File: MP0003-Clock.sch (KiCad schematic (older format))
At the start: 43 parts, among them J1 Conn_01x02, J2 Conn_01x06, J3 Conn_01x06, SW1 HOLD, SW2 SW_Push_DPDT_8x8, SW3 RESET, U1 NE555P, U2 74HC00, U3 74HC00, U4 74HC14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

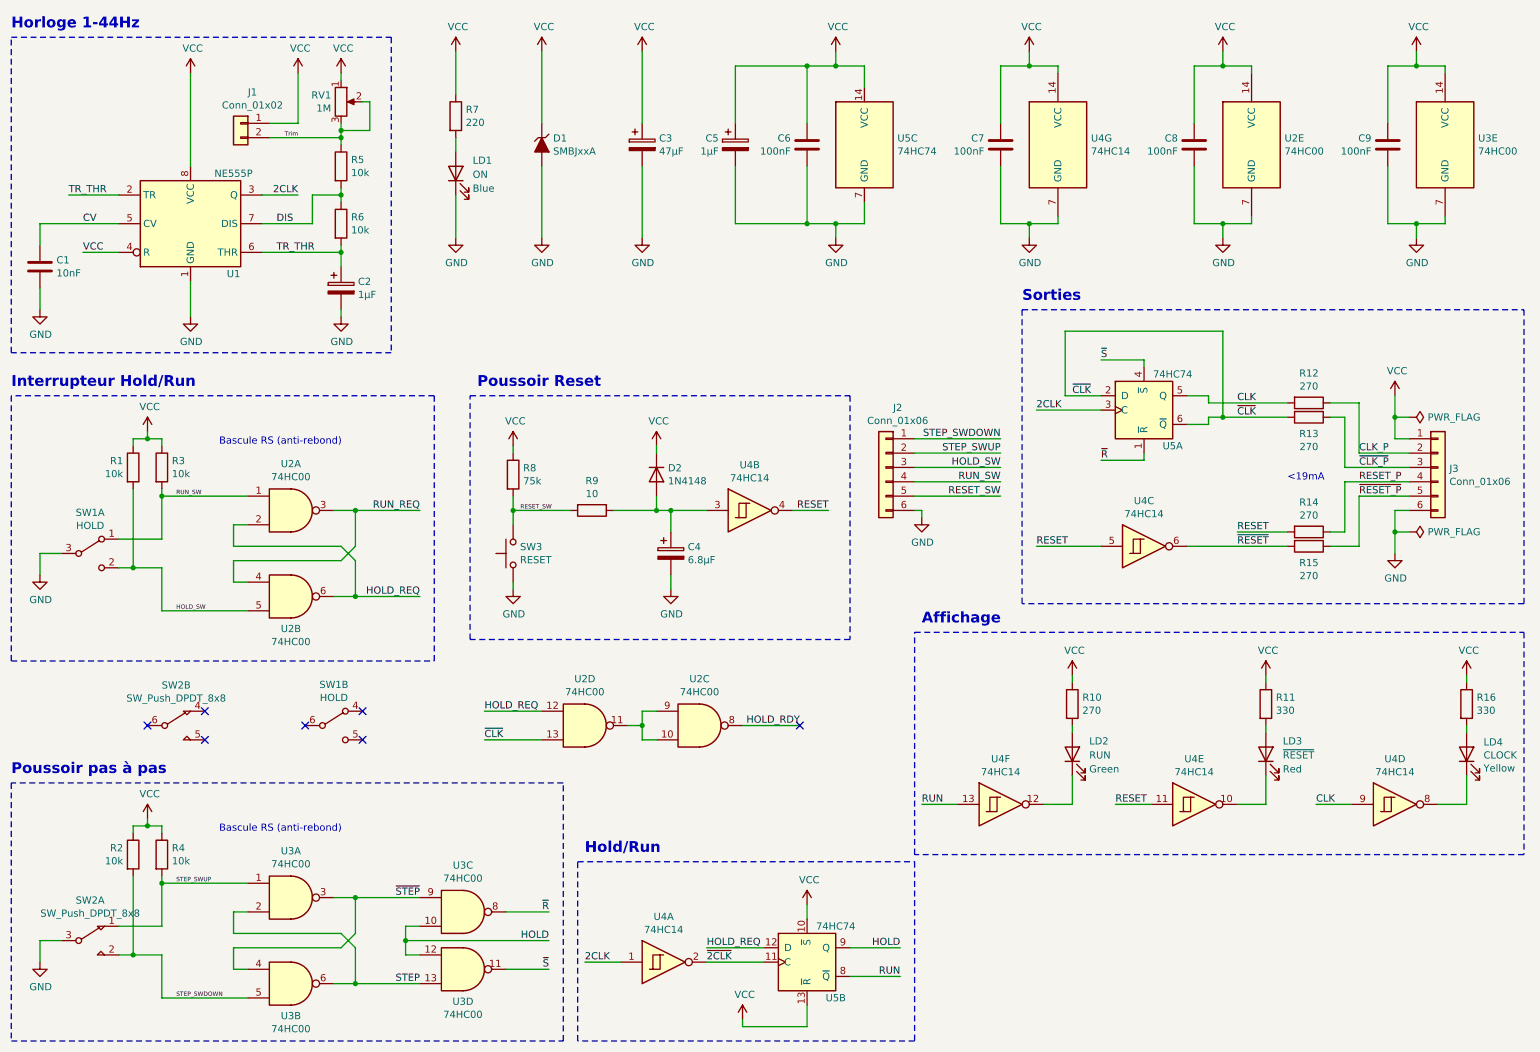
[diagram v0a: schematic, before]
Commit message: Ajout dun fusible réarmable, correction bug basculement mode RUM/HOLD Montage testé et validé sur breadboard. Mesures validées à l'analyseur logique
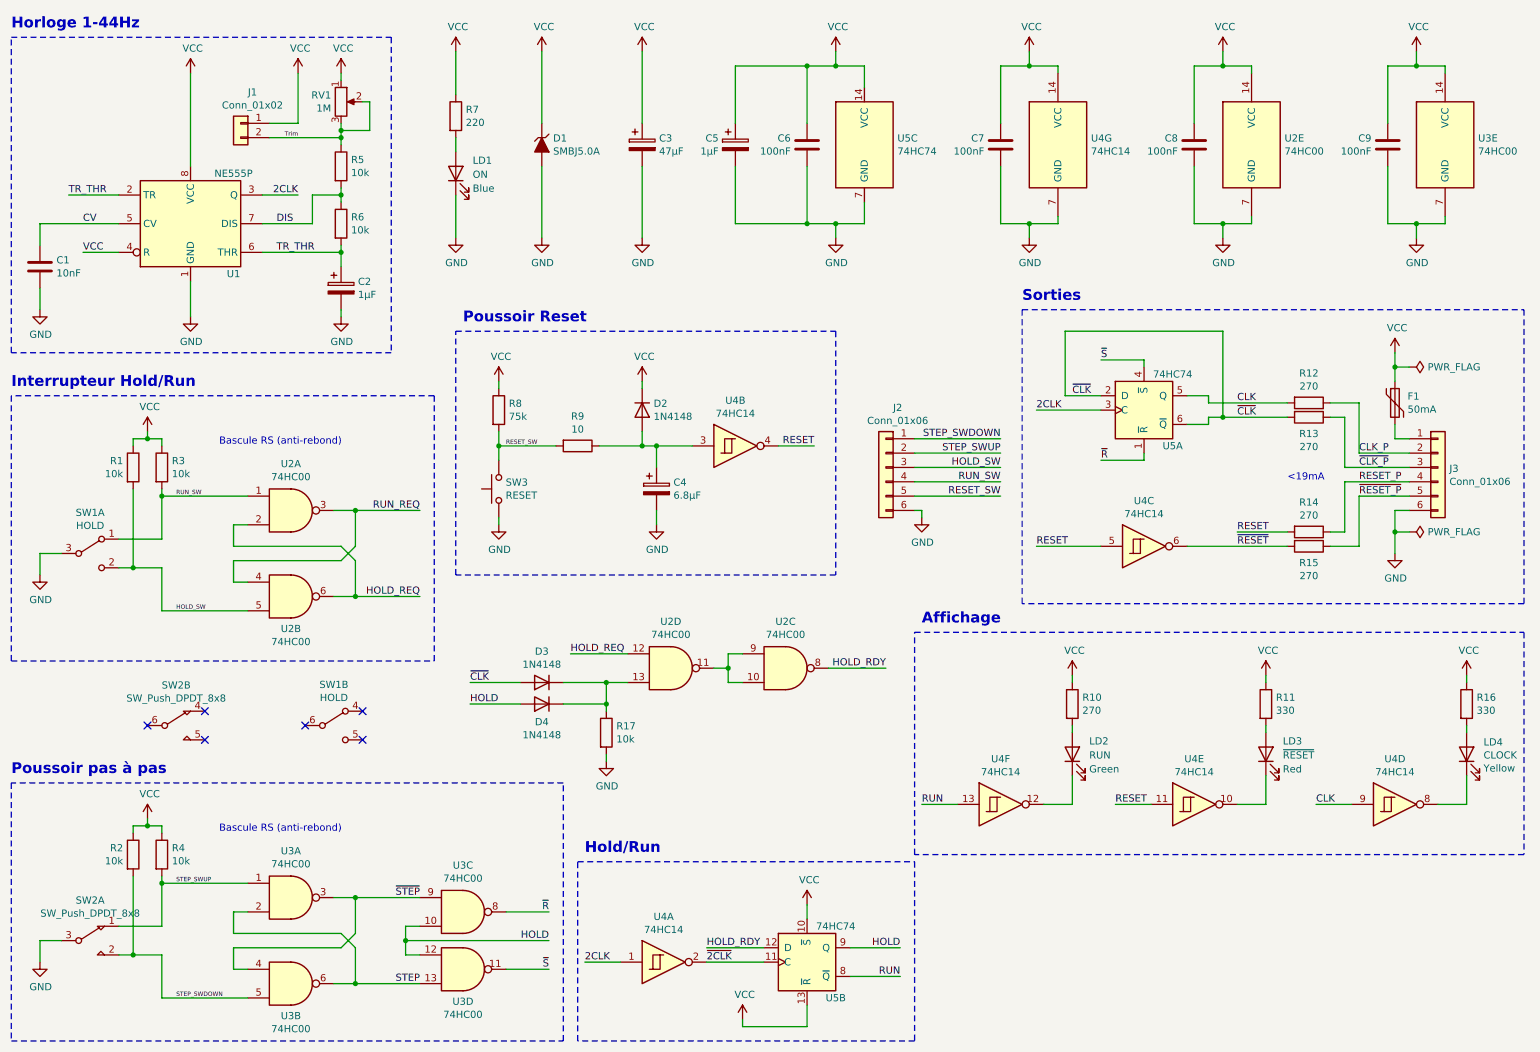
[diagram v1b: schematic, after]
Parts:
- added D3, D4: 1N4148, Diode_THT:D_DO-35_SOD27_P7.62mm_Horizontal, symbol Diode:1N4148
- added F1: 50mA, ValTronix:Fuse_Bourns_CMF-RL1, symbol ValTronix:CMF-RL50A
- added R17: 10k, symbol Device:R
- D1: value SMBJxxA -> SMBJ5.0A
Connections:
- net GND: now also R17.2
- net HOLD: now also D4.2 (A)
- net HOLD_RDY: now also U5.12 (D)
- net HOLD_REQ: no longer U5.12 (D)
- net VCC: now also F1.1; no longer J3.1 (Pin_1)
- net ~CLK: now also D3.2 (A); no longer U2.13
- new net: F1.2, J3.1 (Pin_1)
- new net: D3.1 (K), D4.1 (K), R17.1, U2.13
- no-connect marks 7 -> 6
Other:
- moved on the sheet: C4, D2, R8, R9, SW3, U2C, U2D, U4B

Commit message: Passage à la version 1.0 du plan. Ajout d'un jumper pour utiliser une source externe d'horloge et ajout d'un polyswitch en sécurité. Testé et validé sur breadbord et proto. Note: pas de PCB.
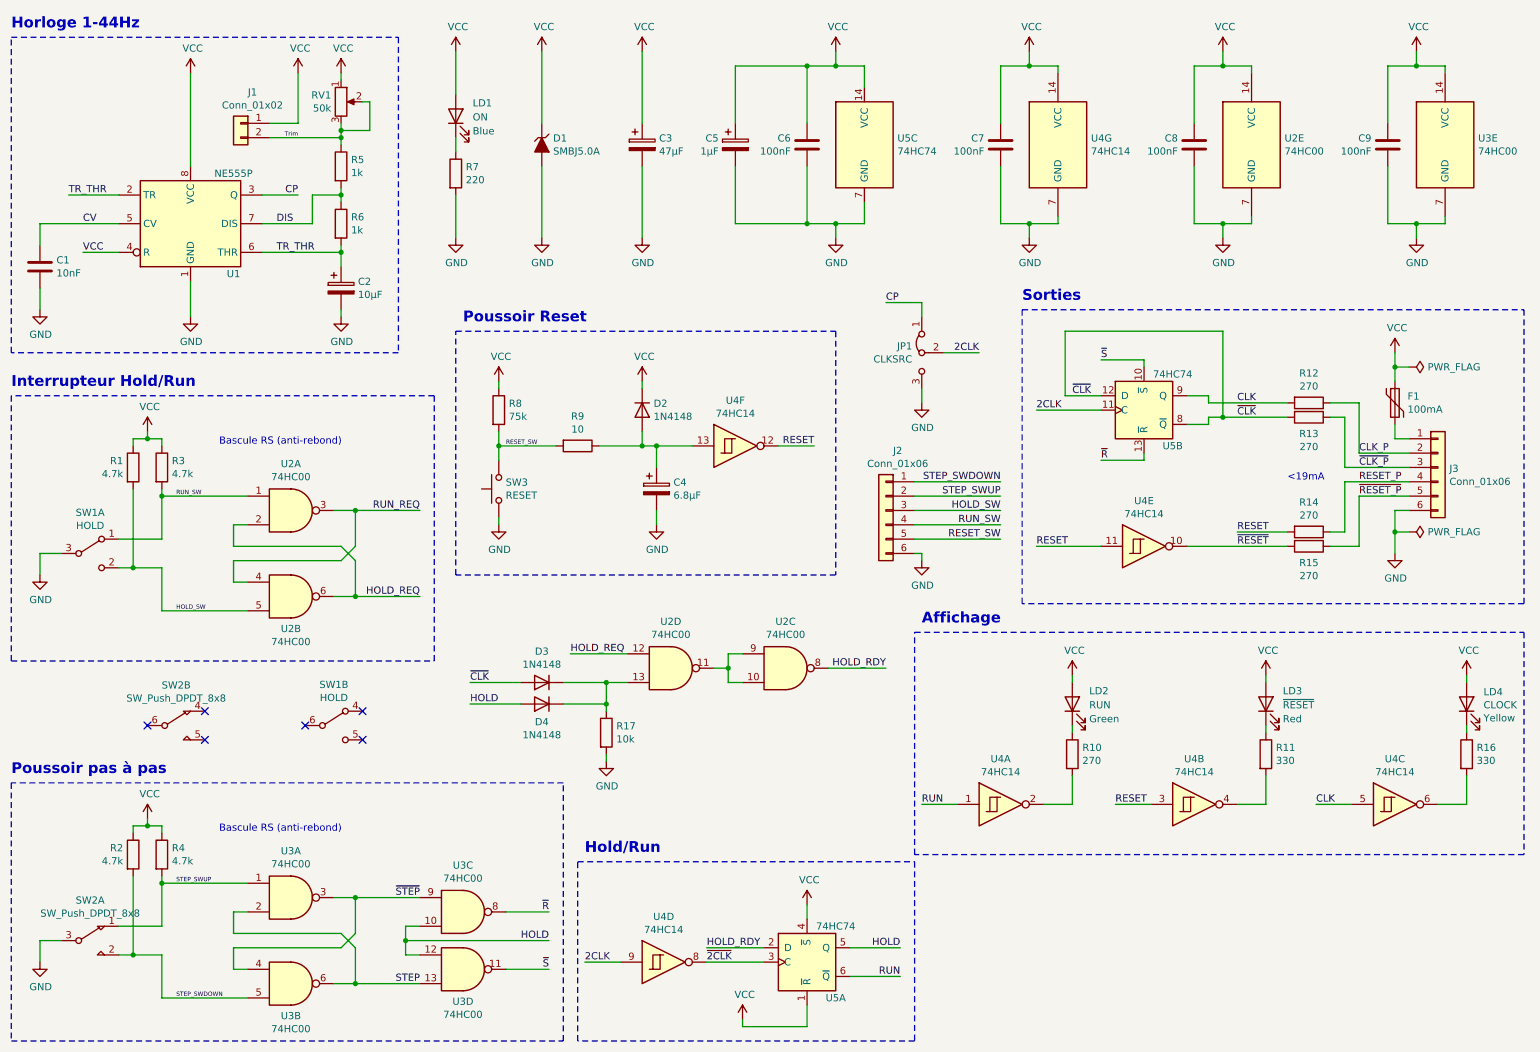
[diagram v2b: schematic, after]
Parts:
- added JP1: CLKSRC, symbol Jumper:Jumper_3_Bridged12
- C2: value 1µF -> 10µF
- F1: value 50mA -> 100mA
- R1, R2, R3, R4: value 10k -> 4.7k
- R5, R6: value 10k -> 1k
- RV1: value 1M -> 50k
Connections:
- net 2CLK: now also U4.9, U5.11 (C), JP1.2 (C); no longer U1.3 (Q), U4.1, U5.3 (C)
- net CLK: now also U4.5, U5.9 (Q); no longer U4.9, U5.5 (Q)
- net GND: now also R7.2, JP1.3 (B); no longer LD1.1 (K)
- net HOLD: now also U5.5 (Q); no longer U5.9 (Q)
- net HOLD_RDY: now also U5.2 (D); no longer U5.12 (D)
- net RESET: now also U4.11, U4.12, U4.3; no longer U4.11, U4.4, U4.5
- net RUN: now also U4.1, U5.6 (~Q); no longer U4.13, U5.8 (~Q)
- net VCC: now also LD1.2 (A), LD2.2 (A), LD3.2 (A), LD4.2 (A), U5.1 (~R), U5.4 (~S); no longer R10.1, R11.1, R16.1, R7.1, U5.10 (~S), U5.13 (~R)
- net ~2CLK: now also U4.8, U5.3 (C); no longer U4.2, U5.11 (C)
- net ~CLK: now also U5.12 (D), U5.8 (~Q); no longer U5.2 (D), U5.6 (~Q)
- net ~R: now also U5.13 (~R); no longer U5.1 (~R)
- net ~RESET: now also U4.10; no longer U4.6
- net ~S: now also U5.10 (~S); no longer U5.4 (~S)
- net at R16.2: now also U4.6; no longer LD4.2 (A)
- net at LD4.1 (K): now also R16.1; no longer U4.8
- net at C4.1, D2.2 (A), R9.1: now also U4.13; no longer U4.3
- net at R11.2: now also U4.4; no longer LD3.2 (A)
- net at LD3.1 (K): now also R11.1; no longer U4.10
- net at LD2.1 (K): now also R10.1; no longer U4.12
- net at R10.2: now also U4.2; no longer LD2.2 (A)
- new net: LD1.1 (K), R7.1
- new net CP: JP1.1 (A), U1.3 (Q)
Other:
- moved on the sheet: J2, LD1, LD2, LD3, LD4, R10, R11, R16, R7

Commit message: Version 1, totalement fonctionnelle avec photos réalisation et documentation
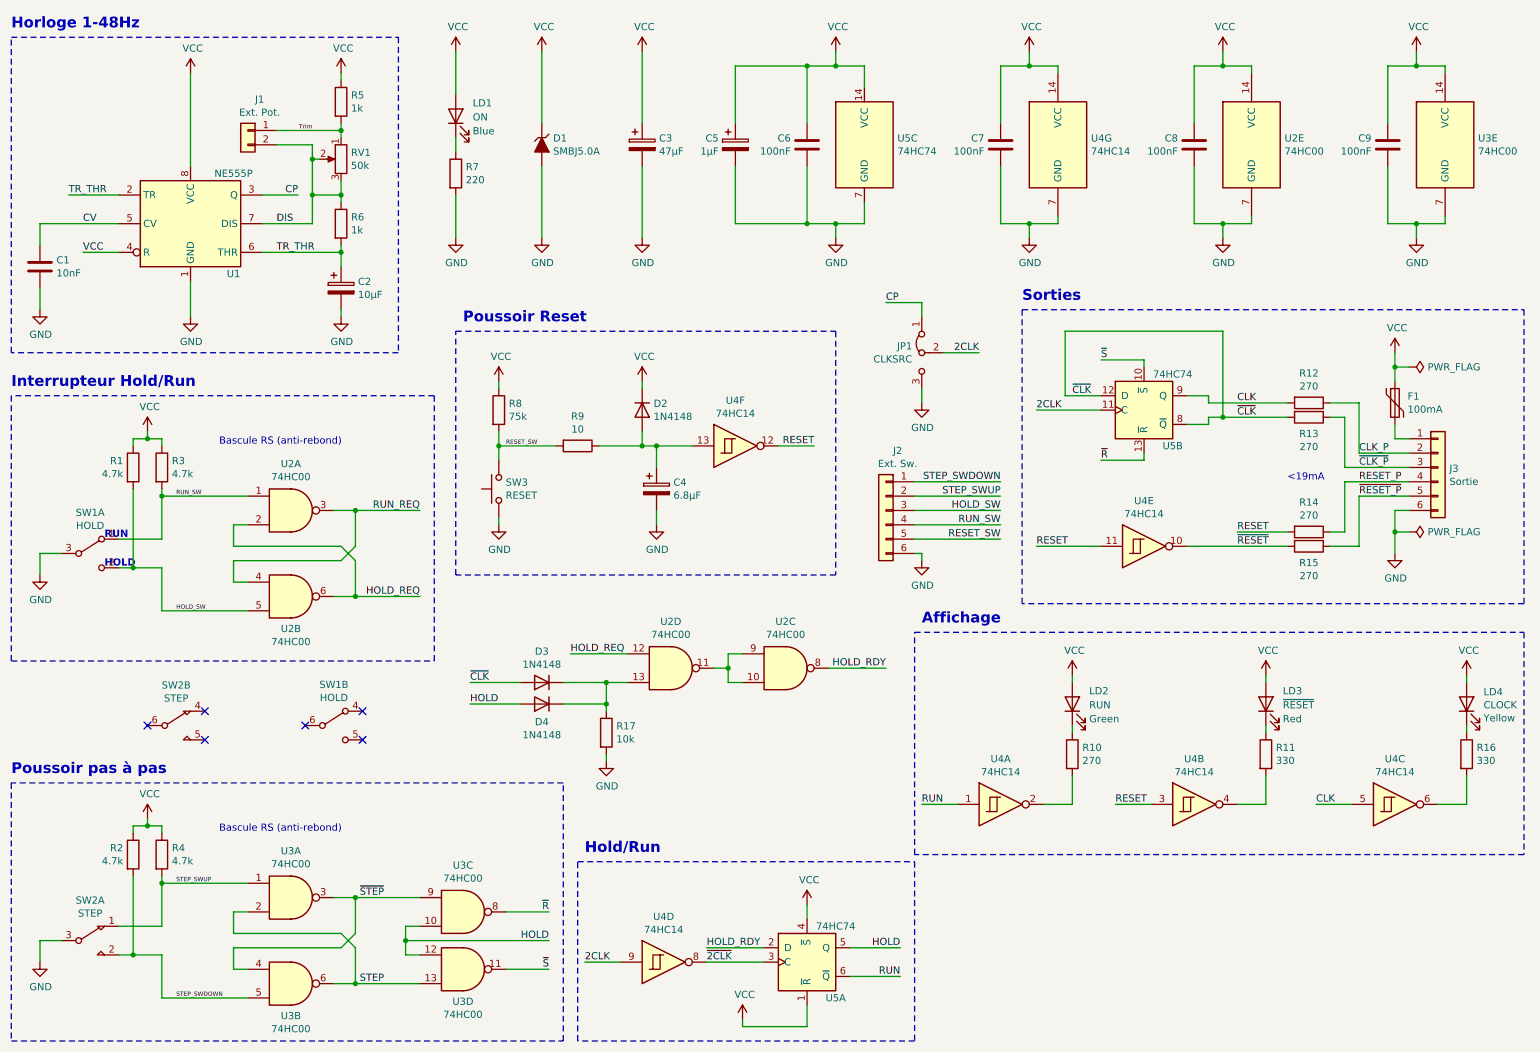
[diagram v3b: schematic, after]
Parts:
- J1: value Conn_01x02 -> Ext. Pot.
- J2: value Conn_01x06 -> Ext. Sw.
- J3: value Conn_01x06 -> Sortie
- SW2: value SW_Push_DPDT_8x8 -> STEP
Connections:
- net DIS: now also J1.2 (Pin_2), RV1.2, RV1.3; no longer R5.2
- net Trim: now also J1.1 (Pin_1), R5.2, RV1.1; no longer J1.2 (Pin_2), R5.1, RV1.2, RV1.3
- net VCC: now also R5.1; no longer J1.1 (Pin_1), RV1.1
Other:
- note added: "HOLD"
- note added: "Horloge 1-48Hz"
- note added: "RUN"
- note removed: "Horloge 1-44Hz"
- moved on the sheet: J1, R5, RV1
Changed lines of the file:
@@
 Rev "1.0"
 Comp "ValTronix"
-Comment1 ""
+Comment1 "JP1 permet de choisir entre la source interne ou externe pour le signal d'horloge."
 Comment2 "Reset à la mise sous tension et lors de l'appui sur le bouton"
-Comment3 "Mode pas à pas sans rebond"
-Comment4 "Horloge débrayable à fréquence variable (ratio 50%)"
+Comment3 "Fréquence max. = 10MHz avec source externe de 20MHz"
+Comment4 "Horloge débrayable à fréquence variable (ratio 50%) - Mode pas à pas sans rebond"
 $EndDescr
 $Comp
@@
 P 10500 3700
 F 0 "J3" H 10580 3692 50  0000 L CNN
-F 1 "Conn_01x06" H 10580 3601 50  0000 L CNN
+F 1 "Sortie" H 10580 3601 50  0000 L CNN
 F 2 "" H 10500 3700 50  0001 C CNN
 F 3 "~" H 10500 3700 50  0001 C CNN
@@
 L Device:R_POT RV1
 U 1 1 63969D46
-P 2850 1150
-F 0 "RV1" H 2781 1196 50  0000 R CNN
-F 1 "50k" H 2781 1105 50  0000 R CNN
-F 2 "" H 2850 1150 50  0001 C CNN
-F 3 "~" H 2850 1150 50  0001 C CNN
-	1    2850 1150
-	1    0    0    -1
+P 2850 1550
+F 0 "RV1" H 2781 1596 50  0000 R CNN
+F 1 "50k" H 2781 1505 50  0000 R CNN
+F 2 "" H 2850 1550 50  0001 C CNN
+F 3 "~" H 2850 1550 50  0001 C CNN
+	1    2850 1550
+	-1   0    0    -1
 $EndComp
 $Comp
@@
 Text Label 1050 2200 0    50   ~ 0
 VCC
-Text Label 3400 7300 2    50   ~ 0
+Text Label 3150 7300 2    50   ~ 0
 STEP
 $Comp
@@
 L Device:R R5
 U 1 1 63CECA9D
-P 2850 1600
-F 0 "R5" H 2920 1646 50  0000 L CNN
-F 1 "1k" H 2920 1555 50  0000 L CNN
-F 2 "" V 2780 1600 50  0001 C CNN
-F 3 "~" H 2850 1600 50  0001 C CNN
-	1    2850 1600
-	1    0    0    -1
-$EndComp
-Wire Wire Line
-	2850 1750 2850 1800
+P 2850 1150
+F 0 "R5" H 2920 1196 50  0000 L CNN
+F 1 "1k" H 2920 1105 50  0000 L CNN
+F 2 "" V 2780 1150 50  0001 C CNN
+F 3 "~" H 2850 1150 50  0001 C CNN
+	1    2850 1150
+	1    0    0    -1
+$EndComp
+Wire Wire Line
+	2850 1700 2850 1800
 Connection ~ 2850 1800
-Wire Wire Line
-	3000 1150 3050 1150
-Wire Wire Line
-	3050 1150 3050 1350
-Wire Wire Line
-	3050 1350 2850 1350
-Wire Wire Line
-	2850 1350 2850 1300
-Wire Wire Line
-	2850 1350 2850 1400
-Connection ~ 2850 1350
 $Comp
 L power:VCC #PWR09
@@
 Text Label 5400 7050 0    50   ~ 0
 HOLD_RDY
-Text Label 3400 6700 2    50   ~ 0
+Text Label 3150 6700 2    50   ~ 0
 ~STEP
 Wire Wire Line
@@
 P 6650 4000
 F 0 "J2" H 6568 4417 50  0000 C CNN
-F 1 "Conn_01x06" H 6568 4326 50  0000 C CNN
+F 1 "Ext. Sw." H 6568 4326 50  0000 C CNN
 F 2 "" H 6650 4000 50  0001 C CNN
 F 3 "~" H 6650 4000 50  0001 C CNN
@@
 P 1100 7000
 F 0 "SW2" H 1100 7281 50  0000 C CNN
-F 1 "SW_Push_DPDT_8x8" H 1100 7190 50  0000 C CNN
+F 1 "STEP" H 1100 7190 50  0000 C CNN
 F 2 "ValTronix:SW_Push_DPDT_8x8mm" H 1100 7000 50  0001 C CNN
 F 3 "~" H 1100 7000 50  0001 C CNN
@@
 P 1700 5500
 F 0 "SW2" H 1700 5781 50  0000 C CNN
-F 1 "SW_Push_DPDT_8x8" H 1700 5690 50  0000 C CNN
+F 1 "STEP" H 1700 5690 50  0000 C CNN
 F 2 "ValTronix:SW_Push_DPDT_8x8mm" H 1700 5500 50  0001 C CNN
 F 3 "~" H 1700 5500 50  0001 C CNN
@@
 NoConn ~ 1500 5500
 Text Notes 550  650  0    75   ~ 15
-Horloge 1-44Hz
+Horloge 1-48Hz
 Wire Notes Line width 10
 	550  700  3250 700
@@
 L Connector_Generic:Conn_01x02 J1
 U 1 1 63D1BB80
-P 2150 1300
-F 0 "J1" H 2068 1517 50  0000 C CNN
-F 1 "Conn_01x02" H 2068 1426 50  0000 C CNN
-F 2 "" H 2150 1300 50  0001 C CNN
-F 3 "~" H 2150 1300 50  0001 C CNN
-	1    2150 1300
+P 2200 1350
+F 0 "J1" H 2118 1567 50  0000 C CNN
+F 1 "Ext. Pot." H 2118 1476 50  0000 C CNN
+F 2 "" H 2200 1350 50  0001 C CNN
+F 3 "~" H 2200 1350 50  0001 C CNN
+	1    2200 1350
 	-1   0    0    -1
 $EndComp
-Wire Wire Line
-	2350 1400 2850 1400
-Connection ~ 2850 1400
-Wire Wire Line
-	2850 1400 2850 1450
-Wire Wire Line
-	2350 1300 2550 1300
-Wire Wire Line
-	2550 1300 2550 950
-$Comp
-L power:VCC #PWR08
-U 1 1 63D64864
-P 2550 950
-F 0 "#PWR08" H 2550 800 50  0001 C CNN
-F 1 "VCC" H 2565 1123 50  0000 C CNN
-F 2 "" H 2550 950 50  0001 C CNN
-F 3 "" H 2550 950 50  0001 C CNN
-	1    2550 950
-	1    0    0    -1
-$EndComp
-Text Label 2550 1400 2    30   ~ 0
+Text Label 2650 1350 2    30   ~ 0
 Trim
 Text Notes 9450 3800 0    50   ~ 0
@@
 Wire Notes Line width 10
 	550  7700 4400 7700
-Wire Notes Line width 10
-	4400 7700 4400 5900
-Wire Notes Line width 10
-	4400 5900 550  5900
 Wire Notes Line width 10
 	3650 2750 6300 2750
@@
 Wire Wire Line
 	6900 2650 6900 2550
+Text Notes 1200 4200 0    50   ~ 10
+RUN
+Text Notes 1200 4400 0    50   ~ 10
+HOLD
+Wire Notes Line width 10
+	4400 7700 4400 5900
+Wire Notes Line width 10
+	4400 5900 550  5900
+Wire Wire Line
+	2850 1300 2850 1350
+Wire Wire Line
+	2400 1450 2650 1450
+Wire Wire Line
+	2650 1450 2650 1550
+Connection ~ 2650 1800
+Wire Wire Line
+	2700 1550 2650 1550
+Connection ~ 2650 1550
+Wire Wire Line
+	2650 1550 2650 1800
+Wire Wire Line
+	2850 1350 2400 1350
+Connection ~ 2850 1350
+Wire Wire Line
+	2850 1350 2850 1400
 $EndSCHEMATC
